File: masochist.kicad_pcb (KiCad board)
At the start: 2 copper layers, 202.4 x 103.2 mm, 87 parts, among them J1 USB_C_Receptacle_USB2.0, J2 AVR-ISP-6, SW1 RESET, SW2 SW_Push, U1 ATmega328P-PU, Y1 Crystal

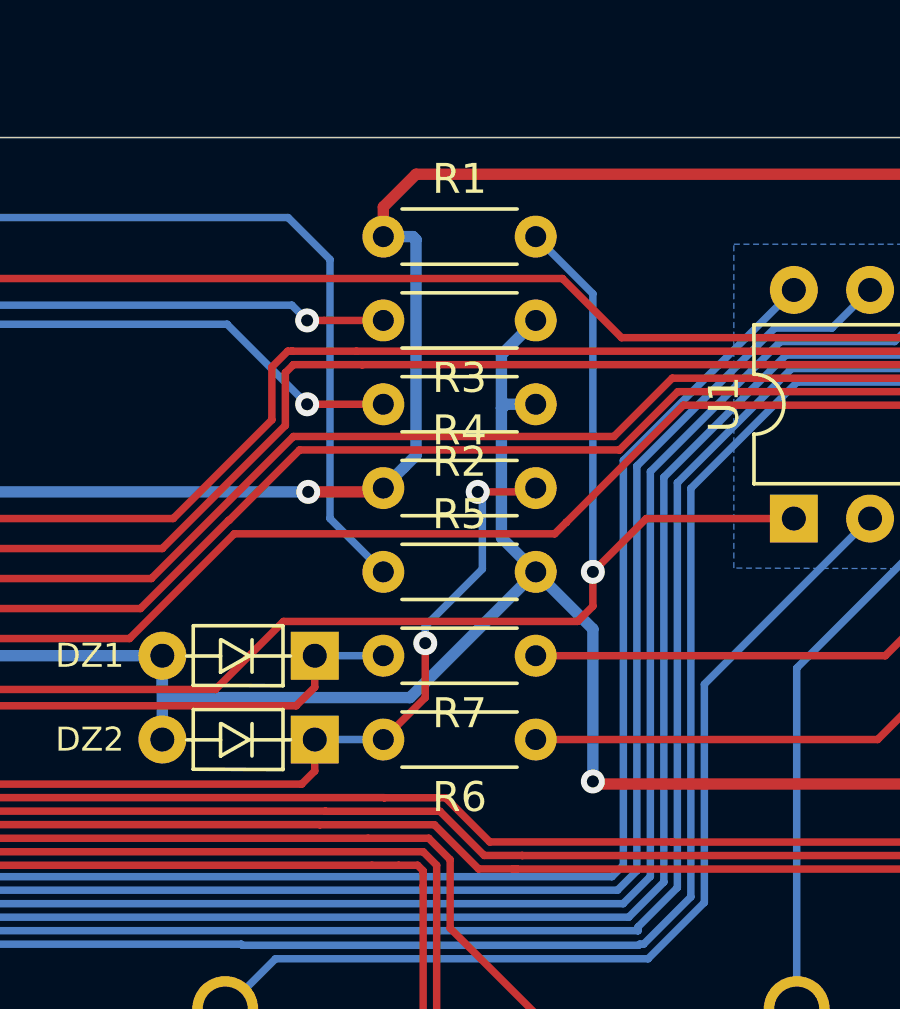
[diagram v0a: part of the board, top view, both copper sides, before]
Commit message: updated silkscreen, regen gerbers
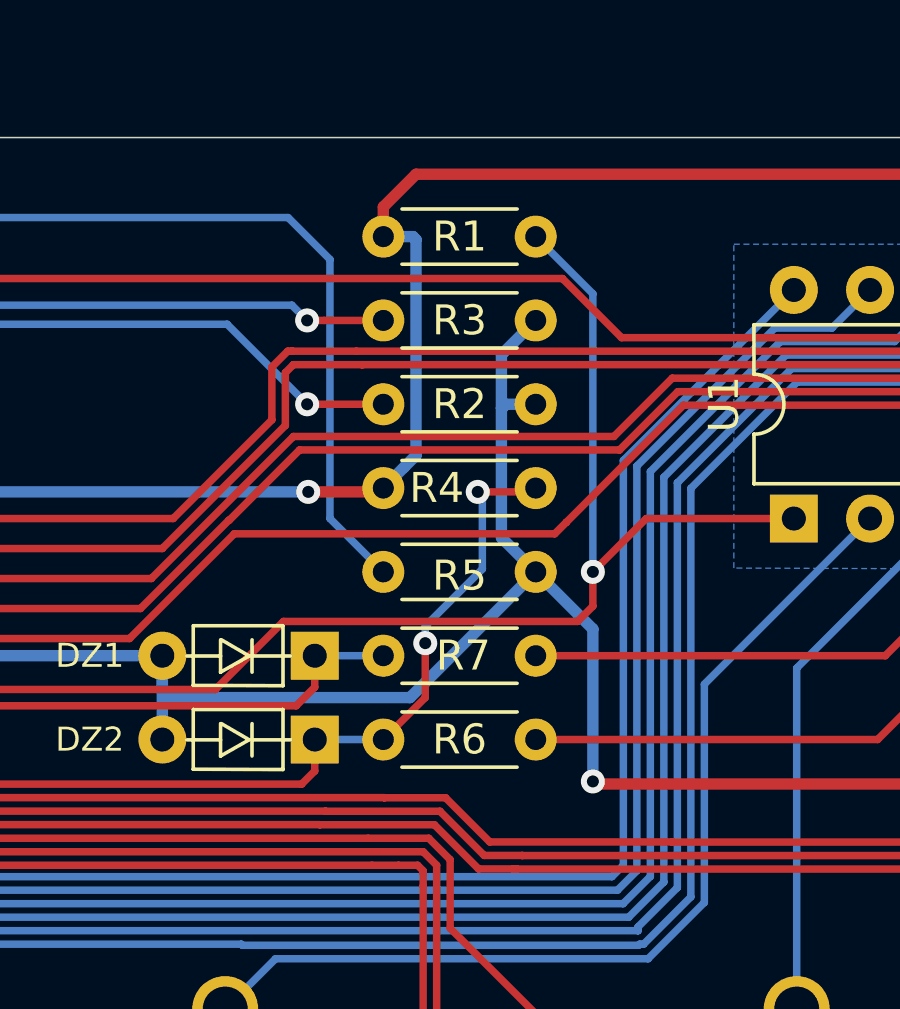
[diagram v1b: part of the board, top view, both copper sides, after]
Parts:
- added G***: LOGO, silkscreen:reid_face_tiny, B.Cu at (168.3, 46.0)

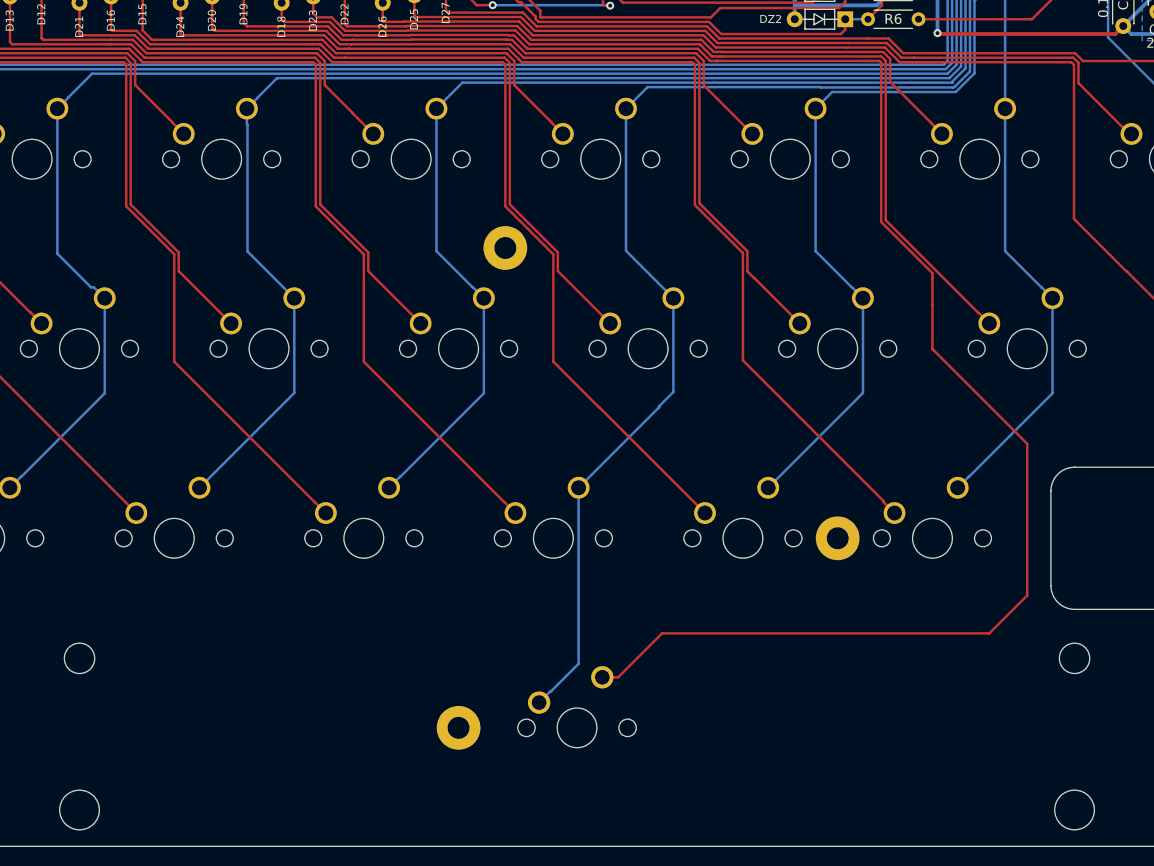
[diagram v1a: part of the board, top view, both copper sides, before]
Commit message: Flipped spacebar and rerouted traces
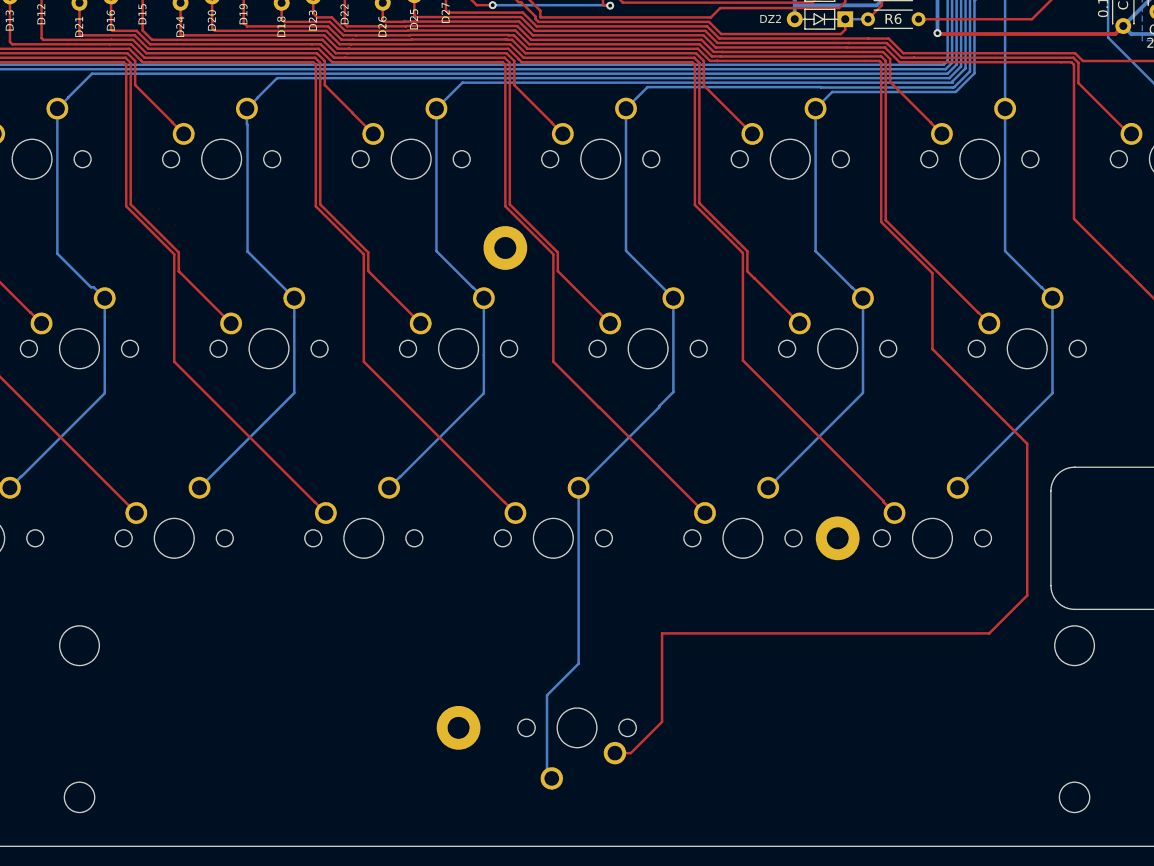
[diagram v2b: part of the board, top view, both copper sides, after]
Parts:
- turned KC_SPC1 to 180 degrees
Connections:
- KC_SPC1 pad 1: COL5 -> Net-(D18-Pad2)
- KC_SPC1 pad 2: Net-(D18-Pad2) -> COL5
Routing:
- net COL5: track 135.9 -> 143.4 mm
- net Net-(D18-Pad2): track 169.6 -> 176.7 mm
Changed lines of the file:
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@@
     (thickness 1.6)
     (drawings 38)
-    (tracks 973)
+    (tracks 968)
     (zones 0)
     (modules 88)
@@
   )
   (module MX_Only:MXOnly-6.25U-NoLED (layer F.Cu)
-    (at 170.65625 123.03125)
+    (at 170.65625 123.03125 180)
     (fp_text reference KC_SPC1 (at 0 3.175) (layer Dwgs.User)
       (effects (font (size 1 1) (thickness 0.15)))
@@
     (fp_line (start -59.53125 9.525) (end 59.53125 9.525) (layer Dwgs.User) (width 0.15))
     (fp_line (start -59.53125 9.525) (end -59.53125 -9.525) (layer Dwgs.User) (width 0.15))
-    (pad 2 thru_hole circle (at 2.54 -5.08) (size 2.25 2.25) (drill 1.47) (layers *.Cu B.Mask)
-      (net 25 "Net-(D18-Pad2)"))
-    (pad "" np_thru_hole circle (at 0 0) (size 3.9878 3.9878) (drill 3.9878) (layers *.Cu *.Mask))
-    (pad 1 thru_hole circle (at -3.81 -2.54) (size 2.25 2.25) (drill 1.47) (layers *.Cu B.Mask)
+    (pad 2 thru_hole circle (at 2.54 -5.08 180) (size 2.25 2.25) (drill 1.47) (layers *.Cu B.Mask)
       (net 46 COL5))
-    (pad "" np_thru_hole circle (at -5.08 0 48.0996) (size 1.75 1.75) (drill 1.75) (layers *.Cu *.Mask))
-    (pad "" np_thru_hole circle (at 5.08 0 48.0996) (size 1.75 1.75) (drill 1.75) (layers *.Cu *.Mask))
-    (pad "" np_thru_hole circle (at -49.9999 -6.985) (size 3.048 3.048) (drill 3.048) (layers *.Cu *.Mask))
-    (pad "" np_thru_hole circle (at 49.9999 -6.985) (size 3.048 3.048) (drill 3.048) (layers *.Cu *.Mask))
-    (pad "" np_thru_hole circle (at -49.9999 8.255) (size 3.9878 3.9878) (drill 3.9878) (layers *.Cu *.Mask))
-    (pad "" np_thru_hole circle (at 49.9999 8.255) (size 3.9878 3.9878) (drill 3.9878) (layers *.Cu *.Mask))
+    (pad "" np_thru_hole circle (at 0 0 180) (size 3.9878 3.9878) (drill 3.9878) (layers *.Cu *.Mask))
+    (pad 1 thru_hole circle (at -3.81 -2.54 180) (size 2.25 2.25) (drill 1.47) (layers *.Cu B.Mask)
+      (net 25 "Net-(D18-Pad2)"))
+    (pad "" np_thru_hole circle (at -5.08 0 228.0996) (size 1.75 1.75) (drill 1.75) (layers *.Cu *.Mask))
+    (pad "" np_thru_hole circle (at 5.08 0 228.0996) (size 1.75 1.75) (drill 1.75) (layers *.Cu *.Mask))
+    (pad "" np_thru_hole circle (at -49.9999 -6.985 180) (size 3.048 3.048) (drill 3.048) (layers *.Cu *.Mask))
+    (pad "" np_thru_hole circle (at 49.9999 -6.985 180) (size 3.048 3.048) (drill 3.048) (layers *.Cu *.Mask))
+    (pad "" np_thru_hole circle (at -49.9999 8.255 180) (size 3.9878 3.9878) (drill 3.9878) (layers *.Cu *.Mask))
+    (pad "" np_thru_hole circle (at 49.9999 8.255 180) (size 3.9878 3.9878) (drill 3.9878) (layers *.Cu *.Mask))
   )
   (module cftkb:SW_PUSH_6mm (layer F.Cu)
@@
   (segment (start 125.654201 54.783971) (end 126.873 56.00277) (width 0.25) (layer F.Cu) (net 24))
   (segment (start 149.225 75.438) (end 149.225 86.233) (width 0.25) (layer F.Cu) (net 24))
-  (segment (start 174.78724 117.95125) (end 179.20049 113.538) (width 0.25) (layer F.Cu) (net 25))
-  (segment (start 173.19625 117.95125) (end 174.78724 117.95125) (width 0.25) (layer F.Cu) (net 25))
-  (segment (start 179.20049 113.538) (end 212.09 113.538) (width 0.25) (layer F.Cu) (net 25))
-  (segment (start 212.09 113.538) (end 215.9 109.728) (width 0.25) (layer F.Cu) (net 25))
-  (segment (start 215.9 109.728) (end 215.9 94.488) (width 0.25) (layer F.Cu) (net 25))
-  (segment (start 215.9 94.488) (end 206.502 85.09) (width 0.25) (layer F.Cu) (net 25))
-  (segment (start 206.502 85.09) (end 206.375 84.963) (width 0.25) (layer F.Cu) (net 25))
-  (segment (start 206.375 84.963) (end 206.375 80.518) (width 0.25) (layer F.Cu) (net 25))
-  (segment (start 206.375 80.518) (end 206.375 77.851) (width 0.25) (layer F.Cu) (net 25))
-  (segment (start 206.375 77.851) (end 206.375 77.34441) (width 0.25) (layer F.Cu) (net 25))
-  (segment (start 206.375 77.34441) (end 201.22599 72.1954) (width 0.25) (layer F.Cu) (net 25))
-  (segment (start 201.22599 72.1954) (end 201.22599 56.7014) (width 0.25) (layer F.Cu) (net 25))
-  (segment (start 201.22599 56.7014) (end 201.22599 56.261) (width 0.25) (layer F.Cu) (net 25))
-  (segment (start 201.22599 56.261) (end 201.22599 56.19199) (width 0.25) (layer F.Cu) (net 25))
-  (segment (start 201.22599 56.19199) (end 201.041 56.007) (width 0.25) (layer F.Cu) (net 25))
-  (segment (start 201.041 56.007) (end 200.406 56.007) (width 0.25) (layer F.Cu) (net 25))
-  (segment (start 200.406 56.007) (end 199.517 56.007) (width 0.25) (layer F.Cu) (net 25))
   (segment (start 184.78077 56.00277) (end 184.785 56.007) (width 0.25) (layer F.Cu) (net 25))
   (segment (start 184.023 56.00277) (end 184.78077 56.00277) (width 0.25) (layer F.Cu) (net 25))
@@
   (segment (start 140.97 50.165) (end 140.97 51.816) (width 0.25) (layer F.Cu) (net 25))
   (segment (start 148.42571 53.42971) (end 148.429942 53.433942) (width 0.25) (layer F.Cu) (net 25))
-  (segment (start 199.517 56.007) (end 184.785 56.007) (width 0.25) (layer F.Cu) (net 25))
   (segment (start 184.785 56.007) (end 184.658 56.007) (width 0.25) (layer F.Cu) (net 25))
   (segment (start 182.804201 54.783971) (end 184.023 56.00277) (width 0.25) (layer F.Cu) (net 25))
@@
   (segment (start 148.429942 53.433942) (end 153.828648 53.433942) (width 0.25) (layer F.Cu) (net 25))
   (segment (start 153.828648 53.433942) (end 153.8646 53.39799) (width 0.25) (layer F.Cu) (net 25))
+  (segment (start 199.517 56.007) (end 184.785 56.007) (width 0.25) (layer F.Cu) (net 25))
+  (segment (start 201.041 56.007) (end 199.517 56.007) (width 0.25) (layer F.Cu) (net 25))
+  (segment (start 212.09 113.538) (end 215.9 109.728) (width 0.25) (layer F.Cu) (net 25))
+  (segment (start 201.22599 56.19199) (end 201.041 56.007) (width 0.25) (layer F.Cu) (net 25))
+  (segment (start 179.20049 122.428) (end 179.20049 113.538) (width 0.25) (layer F.Cu) (net 25))
+  (segment (start 176.05724 125.57125) (end 179.20049 122.428) (width 0.25) (layer F.Cu) (net 25))
+  (segment (start 174.46625 125.57125) (end 176.05724 125.57125) (width 0.25) (layer F.Cu) (net 25))
+  (segment (start 215.9 94.488) (end 206.375 84.963) (width 0.25) (layer F.Cu) (net 25))
+  (segment (start 179.20049 113.538) (end 212.09 113.538) (width 0.25) (layer F.Cu) (net 25))
+  (segment (start 206.375 84.963) (end 206.375 77.34441) (width 0.25) (layer F.Cu) (net 25))
+  (segment (start 215.9 109.728) (end 215.9 94.488) (width 0.25) (layer F.Cu) (net 25))
+  (segment (start 201.22599 72.1954) (end 201.22599 56.19199) (width 0.25) (layer F.Cu) (net 25))
+  (segment (start 206.375 77.34441) (end 201.22599 72.1954) (width 0.25) (layer F.Cu) (net 25))
   (segment (start 152.501991 45.898011) (end 158.091401 45.898011) (width 0.25) (layer B.Cu) (net 26))
   (segment (start 152.190001 46.210001) (end 152.501991 45.898011) (width 0.25) (layer B.Cu) (net 26))
@@
   (segment (start 207.518 56.388) (end 207.899 56.007) (width 0.25) (layer B.Cu) (net 45))
   (segment (start 84.709 56.388) (end 207.518 56.388) (width 0.25) (layer B.Cu) (net 45))
-  (segment (start 167.971249 119.366251) (end 168.034749 119.366251) (width 0.25) (layer B.Cu) (net 46))
-  (segment (start 166.84625 120.49125) (end 167.971249 119.366251) (width 0.25) (layer B.Cu) (net 46))
-  (segment (start 168.034749 119.366251) (end 170.815 116.586) (width 0.25) (layer B.Cu) (net 46))
-  (segment (start 170.815 116.586) (end 170.815 98.90125) (width 0.25) (layer B.Cu) (net 46))
   (segment (start 170.815 98.90125) (end 178.91125 90.805) (width 0.25) (layer B.Cu) (net 46))
   (segment (start 178.91125 90.805) (end 178.91125 90.70975) (width 0.25) (layer B.Cu) (net 46))
@@
   (segment (start 177.740702 58.638048) (end 195.163048 58.638048) (width 0.25) (layer B.Cu) (net 46))
   (segment (start 208.407 58.674) (end 208.442952 58.638048) (width 0.25) (layer B.Cu) (net 46))
+  (segment (start 167.64 127.635) (end 168.11625 128.11125) (width 0.25) (layer B.Cu) (net 46))
+  (segment (start 167.64 119.761) (end 167.64 127.635) (width 0.25) (layer B.Cu) (net 46))
+  (segment (start 170.815 98.90125) (end 170.815 116.586) (width 0.25) (layer B.Cu) (net 46))
+  (segment (start 170.815 116.586) (end 167.64 119.761) (width 0.25) (layer B.Cu) (net 46))
   (segment (start 137.4775 62.356884) (end 137.541 62.420384) (width 0.25) (layer B.Cu) (net 47))
   (segment (start 137.4775 60.80125) (end 137.4775 62.356884) (width 0.25) (layer B.Cu) (net 47))

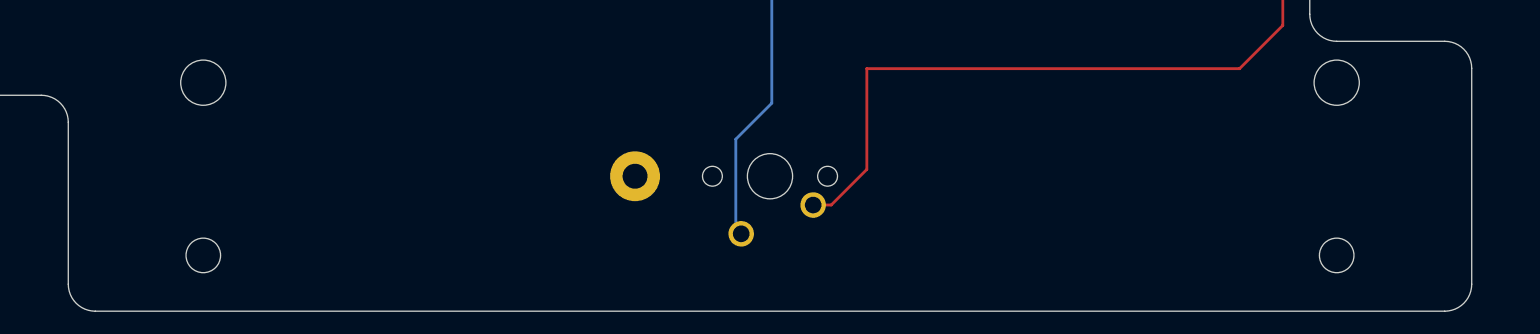
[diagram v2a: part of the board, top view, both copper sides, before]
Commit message: edited edge cuts so the edge is closer to the spacebar stab
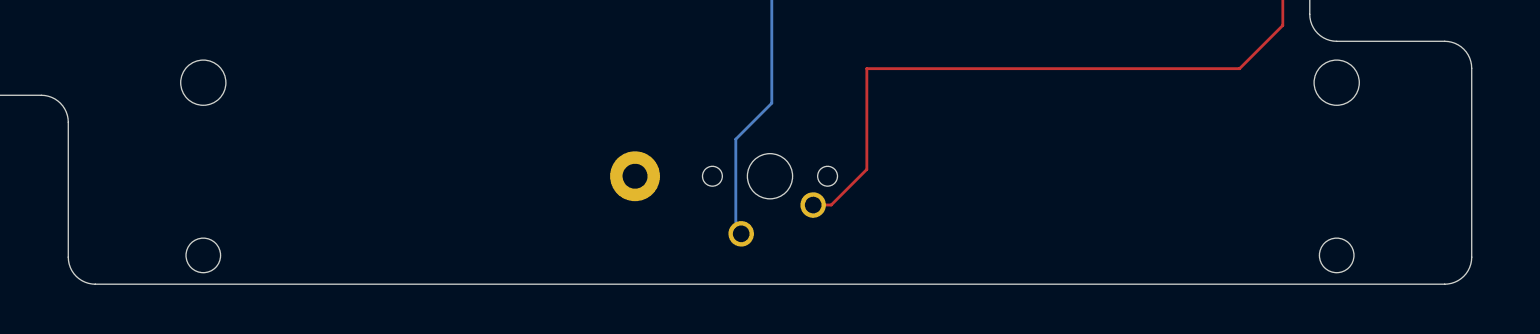
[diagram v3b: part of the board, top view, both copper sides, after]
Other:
- board size 202.4 x 103.2 mm -> 202.4 x 100.8 mm
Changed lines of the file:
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@@
     )
   )
+  (gr_line (start 108.74375 130.175) (end 108.74375 118.26875) (layer Edge.Cuts) (width 0.05))
+  (gr_line (start 232.56875 130.175) (end 232.56875 113.50625) (layer Edge.Cuts) (width 0.05))
   (gr_text "by Reid" (at 213.233 128.016) (layer B.SilkS)
     (effects (font (size 1.5 1.5) (thickness 0.3)) (justify mirror))
@@
   (gr_line (start 218.28125 108.74375) (end 218.28125 99.21875) (layer Edge.Cuts) (width 0.05))
   (gr_line (start 230.1875 111.125) (end 220.6625 111.125) (layer Edge.Cuts) (width 0.05))
-  (gr_line (start 232.56875 132.55625) (end 232.56875 113.50625) (layer Edge.Cuts) (width 0.05))
-  (gr_line (start 111.125 134.9375) (end 230.1875 134.9375) (layer Edge.Cuts) (width 0.05))
+  (gr_line (start 111.125 132.55625) (end 230.1875 132.55625) (layer Edge.Cuts) (width 0.05))
   (gr_arc (start 258.7625 75.40625) (end 258.7625 77.7875) (angle -90) (layer Edge.Cuts) (width 0.05))
   (gr_arc (start 249.2375 80.16875) (end 249.2375 77.7875) (angle -90) (layer Edge.Cuts) (width 0.05))
@@
   (gr_arc (start 220.6625 108.74375) (end 218.28125 108.74375) (angle -90) (layer Edge.Cuts) (width 0.05))
   (gr_arc (start 230.1875 113.50625) (end 232.56875 113.50625) (angle -90) (layer Edge.Cuts) (width 0.05))
-  (gr_arc (start 230.1875 132.55625) (end 230.1875 134.9375) (angle -90) (layer Edge.Cuts) (width 0.05))
-  (gr_line (start 108.74375 118.26875) (end 108.74375 132.55625) (layer Edge.Cuts) (width 0.05))
+  (gr_arc (start 230.1875 130.175) (end 230.1875 132.55625) (angle -90) (layer Edge.Cuts) (width 0.05))
   (gr_line (start 82.55 115.8875) (end 106.3625 115.8875) (layer Edge.Cuts) (width 0.05))
   (gr_line (start 80.16875 99.21875) (end 80.16875 113.50625) (layer Edge.Cuts) (width 0.05))
   (gr_line (start 73.025 96.8375) (end 77.7875 96.8375) (layer Edge.Cuts) (width 0.05))
   (gr_line (start 70.64375 80.16875) (end 70.64375 94.45625) (layer Edge.Cuts) (width 0.05))
-  (gr_arc (start 111.125 132.55625) (end 108.74375 132.55625) (angle -90) (layer Edge.Cuts) (width 0.05))
+  (gr_arc (start 111.125 130.175) (end 108.74375 130.175) (angle -90) (layer Edge.Cuts) (width 0.05))
   (gr_arc (start 106.3625 118.26875) (end 108.74375 118.26875) (angle -90) (layer Edge.Cuts) (width 0.05))
   (gr_arc (start 82.55 113.50625) (end 80.16875 113.50625) (angle -90) (layer Edge.Cuts) (width 0.05))
